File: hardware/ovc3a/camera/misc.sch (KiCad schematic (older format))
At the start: 11 parts, among them CON1 microSD_Card, J5 Conn_02x15_Odd_Even, J6 Conn_02x04_Counter_Clockwise, U9 ARJ11C-MBSAS-A-BA-7MU2

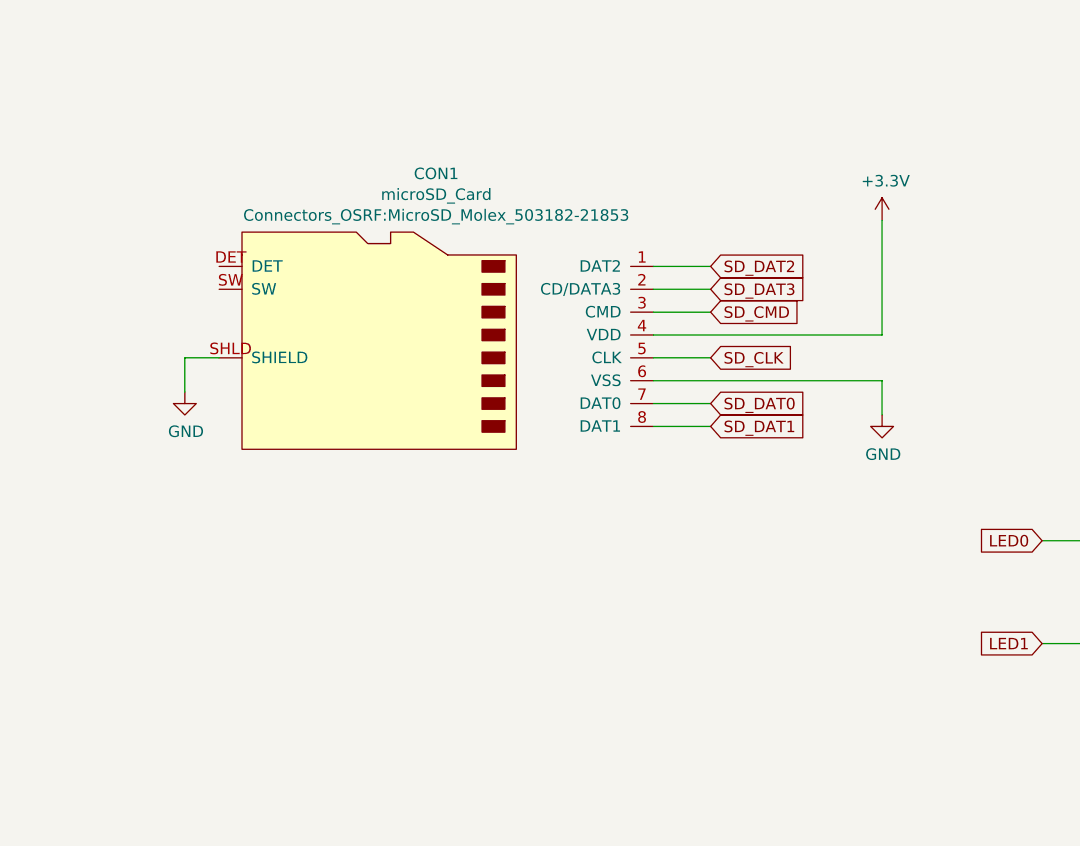
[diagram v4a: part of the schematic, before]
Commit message: switch to in-stock micro-SD connector and do initial pcb route
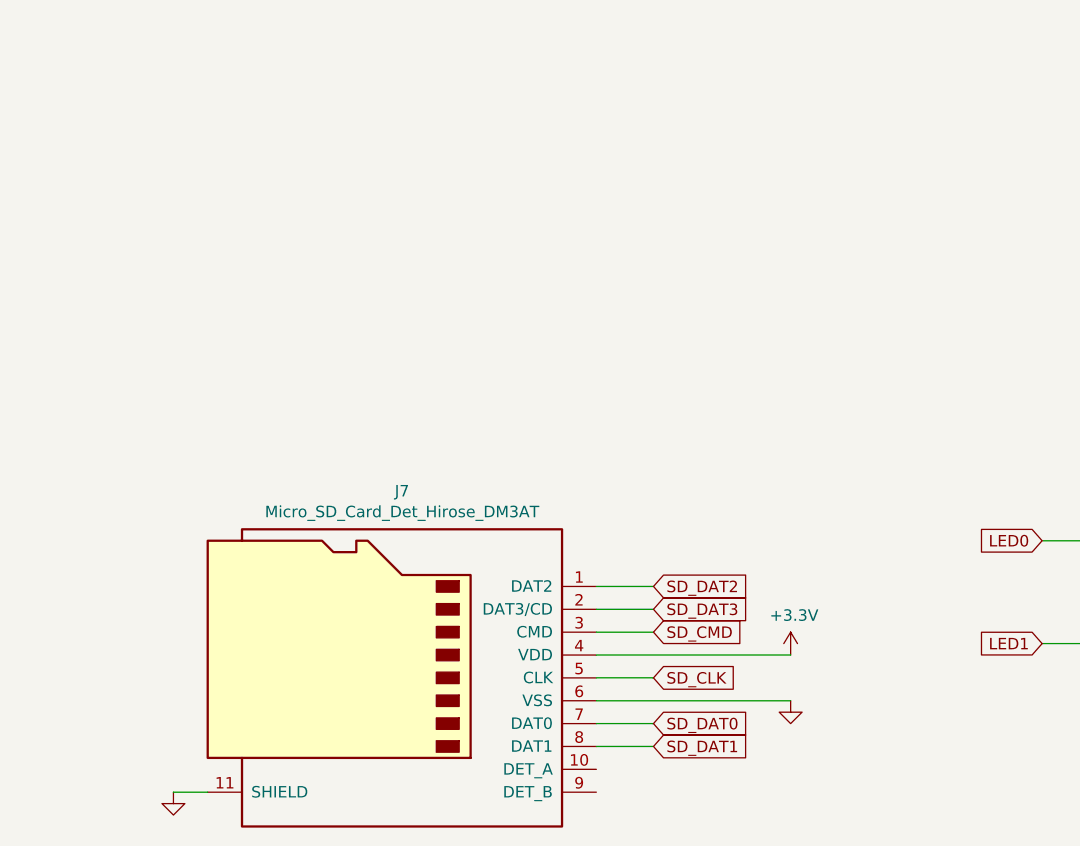
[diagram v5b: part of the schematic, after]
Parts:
- removed CON1: microSD_Card, Connectors_OSRF:MicroSD_Molex_503182-21853, symbol connectors:microSD_Card
- added J7: Micro_SD_Card_Det_Hirose_DM3AT, Connector_Card:microSD_HC_Hirose_DM3AT-SF-PEJM5, symbol Connector:Micro_SD_Card_Det_Hirose_DM3AT
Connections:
- net +3V3: now also J7.4 (VDD)
- net GND: now also J7.11 (SHIELD), J7.6 (VSS)
- net SD_CLK: now also J7.5 (CLK)
- net SD_CMD: now also J7.3 (CMD)
- net SD_DAT0: now also J7.7 (DAT0)
- net SD_DAT1: now also J7.8 (DAT1)
- net SD_DAT2: now also J7.1 (DAT2)
- net SD_DAT3: now also J7.2 (DAT3/CD)
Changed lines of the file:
@@
-	1    0    0    -1
-$EndComp
-$Comp
-L connectors:microSD_Card CON?
-U 1 1 5C477F77
-P 2250 4750
-AR Path="/5C4799A5/5C477F77" Ref="CON?"  Part="1"
-AR Path="/5C470144/5C477F77" Ref="CON1"  Part="1"
-F 0 "CON1" H 2500 5455 50  0000 C CNN
-F 1 "microSD_Card" H 2500 5364 50  0000 C CNN
-F 2 "Connectors_OSRF:MicroSD_Molex_503182-21853" H 2500 5273 50  0000 C CNN
-F 3 "http://www.molex.com/webdocs/datasheets/pdf/en-us/5031821853_MEMORY_CARD_SOCKET.pdf" H 2450 4750 50  0001 C CNN
-F 4 "_" H 2250 4750 50  0001 C CNN "MFN"
-F 5 "_" H 2250 4750 50  0001 C CNN "MFP"
-F 6 "digikey" H 2250 4750 50  0001 C CNN "D1"
-F 7 "mouser" H 2250 4750 50  0001 C CNN "D2"
-F 8 "_" H 2250 4750 50  0001 C CNN "D1PN"
-F 9 "_" H 2250 4750 50  0001 C CNN "D1PL"
-F 10 "_" H 2250 4750 50  0001 C CNN "D2PN"
-F 11 "_" H 2250 4750 50  0001 C CNN "D2PL"
-F 12 "_" H 2250 4750 50  0001 C CNN "Package"
-F 13 "_" H 2250 4750 50  0001 C CNN "Description"
-F 14 "_" H 2250 4750 50  0001 C CNN "Voltage"
-F 15 "_" H 2250 4750 50  0001 C CNN "Power"
-F 16 "_" H 2250 4750 50  0001 C CNN "Tolerance"
-F 17 "_" H 2250 4750 50  0001 C CNN "Temperature"
-F 18 "_" H 2250 4750 50  0001 C CNN "ReverseVoltage"
-F 19 "_" H 2250 4750 50  0001 C CNN "ForwardVoltage"
-F 20 "_" H 2250 4750 50  0001 C CNN "Cont.Current"
-F 21 "_" H 2250 4750 50  0001 C CNN "Frequency"
-F 22 "_" H 2250 4750 50  0001 C CNN "ResonnanceFreq"
-	1    2250 4750
 	1    0    0    -1
 $EndComp
@@
 	3400 1400 3400 1250
 Wire Wire Line
-	3700 4450 3450 4450
-Wire Wire Line
-	3700 4550 3450 4550
-Wire Wire Line
-	3700 4650 3450 4650
-Wire Wire Line
-	3700 5150 3450 5150
-Wire Wire Line
-	3700 5050 3450 5050
-Wire Wire Line
-	3700 4850 3450 4850
-$Comp
-L power:GND #PWR0117
-U 1 1 5C49A0AD
-P 4450 5100
-F 0 "#PWR0117" H 4450 4850 50  0001 C CNN
-F 1 "GND" H 4455 4927 50  0000 C CNN
-F 2 "" H 4450 5100 50  0001 C CNN
-F 3 "" H 4450 5100 50  0001 C CNN
-	1    4450 5100
-	1    0    0    -1
-$EndComp
-Wire Wire Line
-	3450 4750 4450 4750
-Wire Wire Line
-	3450 4950 4450 4950
-Wire Wire Line
-	4450 4950 4450 5100
-$Comp
-L power:GND #PWR0119
-U 1 1 5C49BFA5
-P 1400 5000
-F 0 "#PWR0119" H 1400 4750 50  0001 C CNN
-F 1 "GND" H 1405 4827 50  0000 C CNN
-F 2 "" H 1400 5000 50  0001 C CNN
-F 3 "" H 1400 5000 50  0001 C CNN
-	1    1400 5000
-	1    0    0    -1
-$EndComp
-Wire Wire Line
-	1550 4850 1400 4850
-Wire Wire Line
-	1400 4850 1400 5000
-Wire Wire Line
-	4450 4250 4450 4750
-Text GLabel 3700 4450 2    50   Input ~ 0
+	3450 5850 3200 5850
+Wire Wire Line
+	3450 5950 3200 5950
+Wire Wire Line
+	3450 6050 3200 6050
+Wire Wire Line
+	3450 6550 3200 6550
+Wire Wire Line
+	3450 6450 3200 6450
+Wire Wire Line
+	3450 6250 3200 6250
+Wire Wire Line
+	3200 6150 4050 6150
+Wire Wire Line
+	3200 6350 4050 6350
+Text GLabel 3450 5850 2    50   Input ~ 0
 SD_DAT2
-Text GLabel 3700 4550 2    50   Input ~ 0
+Text GLabel 3450 5950 2    50   Input ~ 0
 SD_DAT3
-Text GLabel 3700 4650 2    50   Input ~ 0
+Text GLabel 3450 6050 2    50   Input ~ 0
 SD_CMD
-Text GLabel 3700 4850 2    50   Input ~ 0
+Text GLabel 3450 6250 2    50   Input ~ 0
 SD_CLK
-Text GLabel 3700 5050 2    50   Input ~ 0
+Text GLabel 3450 6450 2    50   Input ~ 0
 SD_DAT0
-Text GLabel 3700 5150 2    50   Input ~ 0
+Text GLabel 3450 6550 2    50   Input ~ 0
 SD_DAT1
 Text GLabel 3300 1800 2    50   Input ~ 0
@@
 L power:+3.3V #PWR0118
 U 1 1 5C4E6A5A
-P 4450 4250
-F 0 "#PWR0118" H 4450 4100 50  0001 C CNN
-F 1 "+3.3V" H 4465 4423 50  0000 C CNN
-F 2 "" H 4450 4250 50  0001 C CNN
-F 3 "" H 4450 4250 50  0001 C CNN
-	1    4450 4250
+P 4050 6150
+F 0 "#PWR0118" H 4050 6000 50  0001 C CNN
+F 1 "+3.3V" H 4065 6323 50  0000 C CNN
+F 2 "" H 4050 6150 50  0001 C CNN
+F 3 "" H 4050 6150 50  0001 C CNN
+	1    4050 6150
 	1    0    0    -1
 $EndComp
@@
 Text GLabel 7400 3150 2    50   Input ~ 0
 GPIO18
+$Comp
+L Connector:Micro_SD_Card_Det_Hirose_DM3AT J7
+U 1 1 5C4D360F
+P 2300 6250
+F 0 "J7" H 2250 7067 50  0000 C CNN
+F 1 "Micro_SD_Card_Det_Hirose_DM3AT" H 2250 6976 50  0000 C CNN
+F 2 "Connector_Card:microSD_HC_Hirose_DM3AT-SF-PEJM5" H 4350 6950 50  0001 C CNN
+F 3 "https://www.hirose.com/product/en/download_file/key_name/DM3/category/Catalog/doc_file_id/49662/?file_category_id=4&item_id=195&is_series=1" H 2300 6350 50  0001 C CNN
+F 4 "DM3AT-SF-PEJM5" H 2300 6250 50  0001 C CNN "MPN"
+	1    2300 6250
+	-1   0    0    -1
+$EndComp
+$Comp
+L power:GND #PWR0117
+U 1 1 5C49A0AD
+P 4050 6350
+F 0 "#PWR0117" H 4050 6100 50  0001 C CNN
+F 1 "GND" H 4055 6177 50  0001 C CNN
+F 2 "" H 4050 6350 50  0001 C CNN
+F 3 "" H 4050 6350 50  0001 C CNN
+	1    4050 6350
+	1    0    0    -1
+$EndComp
+$Comp
+L power:GND #PWR0119
+U 1 1 5C4F8C21
+P 1350 6750
+F 0 "#PWR0119" H 1350 6500 50  0001 C CNN
+F 1 "GND" H 1355 6577 50  0001 C CNN
+F 2 "" H 1350 6750 50  0001 C CNN
+F 3 "" H 1350 6750 50  0001 C CNN
+	1    1350 6750
+	1    0    0    -1
+$EndComp
+Wire Wire Line
+	1350 6750 1500 6750
 $EndSCHEMATC

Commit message: ovc3a camera pcb work
 * ignore fp-info-cache files
 * reduce size of enet led resistors to 0403.
 * route enet and micro-sd interfaces
 * align lens holders to 90 degrees
 * push outer imagers down a bit to reduce width of pcb to 138mm
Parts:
- C10: footprint Capacitor_SMD:C_0402_1005Metric -> Capacitor_SMD:C_0603_1608Metric
- R12, R13, R14, R15: footprint Resistor_SMD:R_0603_1608Metric -> Resistor_SMD:R_0402_1005Metric
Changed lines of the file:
@@
 F 0 "C10" H 3492 1196 50  0000 L CNN
 F 1 "100n" H 3492 1105 50  0000 L CNN
-F 2 "Capacitor_SMD:C_0402_1005Metric" H 3400 1150 50  0001 C CNN
+F 2 "Capacitor_SMD:C_0603_1608Metric" H 3400 1150 50  0001 C CNN
 F 3 "~" H 3400 1150 50  0001 C CNN
 	1    3400 1150
@@
 F 0 "R13" V 1304 2250 50  0000 C CNN
 F 1 "220R" V 1395 2250 50  0000 C CNN
-F 2 "Resistor_SMD:R_0603_1608Metric" H 1500 2250 50  0001 C CNN
+F 2 "Resistor_SMD:R_0402_1005Metric" H 1500 2250 50  0001 C CNN
 F 3 "~" H 1500 2250 50  0001 C CNN
 	1    1500 2250
@@
 F 0 "R12" V 1304 1700 50  0000 C CNN
 F 1 "220R" V 1395 1700 50  0000 C CNN
-F 2 "Resistor_SMD:R_0603_1608Metric" H 1500 1700 50  0001 C CNN
+F 2 "Resistor_SMD:R_0402_1005Metric" H 1500 1700 50  0001 C CNN
 F 3 "~" H 1500 1700 50  0001 C CNN
 	1    1500 1700
@@
 F 0 "R14" V 5254 5650 50  0000 C CNN
 F 1 "220R" V 5345 5650 50  0000 C CNN
-F 2 "Resistor_SMD:R_0603_1608Metric" H 5450 5650 50  0001 C CNN
+F 2 "Resistor_SMD:R_0402_1005Metric" H 5450 5650 50  0001 C CNN
 F 3 "~" H 5450 5650 50  0001 C CNN
 	1    5450 5650
@@
 F 0 "R15" V 5254 6100 50  0000 C CNN
 F 1 "220R" V 5345 6100 50  0000 C CNN
-F 2 "Resistor_SMD:R_0603_1608Metric" H 5450 6100 50  0001 C CNN
+F 2 "Resistor_SMD:R_0402_1005Metric" H 5450 6100 50  0001 C CNN
 F 3 "~" H 5450 6100 50  0001 C CNN
 	1    5450 6100

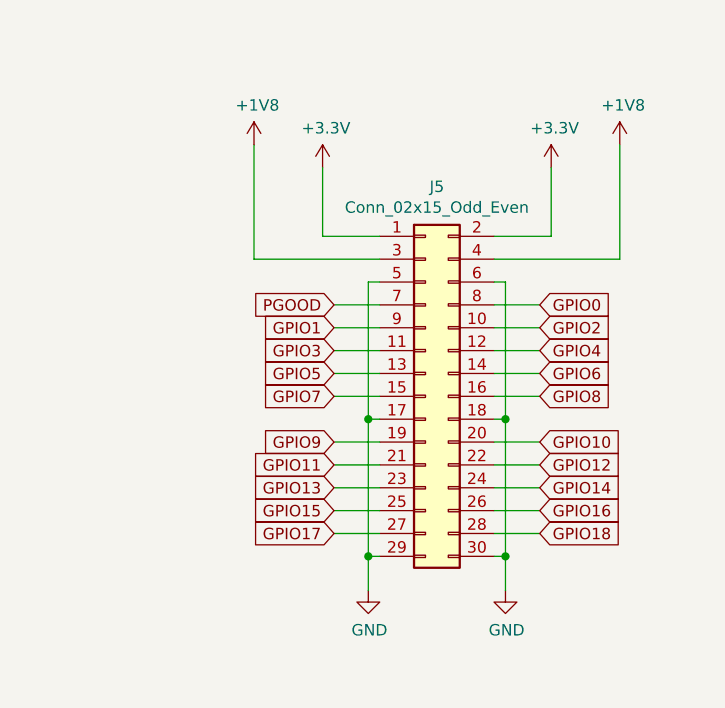
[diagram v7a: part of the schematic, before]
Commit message: Preliminary placement of MIPI lanes, finished routing first imager
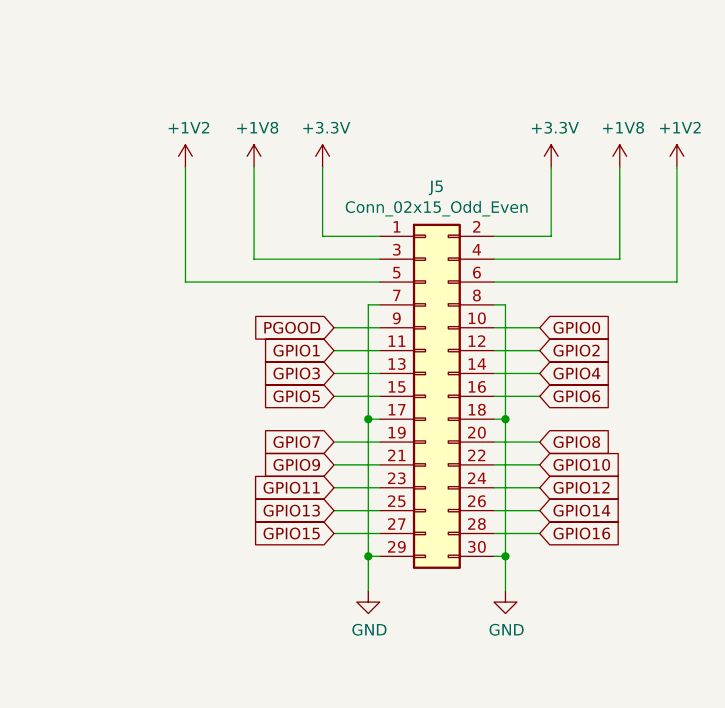
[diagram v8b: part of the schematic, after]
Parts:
- J6: footprint Connector_PinSocket_2.00mm:PinSocket_2x04_P2.00mm_Vertical -> Connector_PinSocket_2.00mm:PinSocket_2x04_P2.00mm_Horizontal
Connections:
- net GPIO17 is gone; now on net GPIO15: J5.27 (Pin_27)
- net GPIO18 is gone; now on net GPIO16: J5.28 (Pin_28)
- net GND: now also J5.7 (Pin_7), J5.8 (Pin_8); no longer J5.5 (Pin_5), J5.6 (Pin_6)
- net GPIO0: now also J5.10 (Pin_10); no longer J5.8 (Pin_8)
- net GPIO1: now also J5.11 (Pin_11); no longer J5.9 (Pin_9)
- net GPIO10: now also J5.22 (Pin_22); no longer J5.20 (Pin_20)
- net GPIO11: now also J5.23 (Pin_23); no longer J5.21 (Pin_21)
- net GPIO12: now also J5.24 (Pin_24); no longer J5.22 (Pin_22)
- net GPIO13: now also J5.25 (Pin_25); no longer J5.23 (Pin_23)
- net GPIO14: now also J5.26 (Pin_26); no longer J5.24 (Pin_24)
- net GPIO15: no longer J5.25 (Pin_25)
- net GPIO16: no longer J5.26 (Pin_26)
- net GPIO2: now also J5.12 (Pin_12); no longer J5.10 (Pin_10)
- net GPIO3: now also J5.13 (Pin_13); no longer J5.11 (Pin_11)
- net GPIO4: now also J5.14 (Pin_14); no longer J5.12 (Pin_12)
- net GPIO5: now also J5.15 (Pin_15); no longer J5.13 (Pin_13)
- net GPIO6: now also J5.16 (Pin_16); no longer J5.14 (Pin_14)
- net GPIO7: now also J5.19 (Pin_19); no longer J5.15 (Pin_15)
- net GPIO8: now also J5.20 (Pin_20); no longer J5.16 (Pin_16)
- net GPIO9: now also J5.21 (Pin_21); no longer J5.19 (Pin_19)
- net PGOOD: now also J5.9 (Pin_9); no longer J5.7 (Pin_7)
- new net +1V2: J5.5 (Pin_5), J5.6 (Pin_6)
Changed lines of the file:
@@
 L power:+1V8 #PWR0140
 U 1 1 5C522639
-P 6150 1450
-F 0 "#PWR0140" H 6150 1300 50  0001 C CNN
-F 1 "+1V8" H 6165 1623 50  0000 C CNN
-F 2 "" H 6150 1450 50  0001 C CNN
-F 3 "" H 6150 1450 50  0001 C CNN
-	1    6150 1450
+P 6150 1550
+F 0 "#PWR0140" H 6150 1400 50  0001 C CNN
+F 1 "+1V8" H 6165 1723 50  0000 C CNN
+F 2 "" H 6150 1550 50  0001 C CNN
+F 3 "" H 6150 1550 50  0001 C CNN
+	1    6150 1550
 	1    0    0    -1
 $EndComp
@@
 L power:+1V8 #PWR0141
 U 1 1 5C522CA8
-P 7750 1450
-F 0 "#PWR0141" H 7750 1300 50  0001 C CNN
-F 1 "+1V8" H 7765 1623 50  0000 C CNN
-F 2 "" H 7750 1450 50  0001 C CNN
-F 3 "" H 7750 1450 50  0001 C CNN
-	1    7750 1450
+P 7750 1550
+F 0 "#PWR0141" H 7750 1400 50  0001 C CNN
+F 1 "+1V8" H 7765 1723 50  0000 C CNN
+F 2 "" H 7750 1550 50  0001 C CNN
+F 3 "" H 7750 1550 50  0001 C CNN
+	1    7750 1550
 	1    0    0    -1
 $EndComp
@@
 	7200 1950 7750 1950
 Wire Wire Line
-	7750 1950 7750 1450
-Wire Wire Line
 	6700 1950 6150 1950
-Wire Wire Line
-	6150 1950 6150 1450
 $Comp
 L power:GND #PWR0143
@@
 	1    0    0    -1
 $EndComp
-Text GLabel 6500 2150 0    50   Input ~ 0
+Text GLabel 6500 2250 0    50   Input ~ 0
 PGOOD
-Wire Wire Line
-	6650 2050 6650 2650
-Wire Wire Line
-	6650 2050 6700 2050
 Wire Wire Line
 	6700 2650 6650 2650
@@
 Wire Wire Line
 	6650 3250 6650 3400
-Wire Wire Line
-	7250 2050 7250 2650
 $Comp
 L power:GND #PWR0142
@@
 Connection ~ 7250 2650
 Wire Wire Line
-	7250 2650 7250 3250
-Wire Wire Line
-	7200 2050 7250 2050
-Wire Wire Line
-	6700 2150 6500 2150
+	6700 2250 6500 2250
 Wire Wire Line
 	6700 1850 6450 1850
@@
 F 0 "J6" H 7100 5100 50  0000 C CNN
 F 1 "Conn_02x04_Counter_Clockwise" H 7400 5000 50  0000 C CNN
-F 2 "Connector_PinSocket_2.00mm:PinSocket_2x04_P2.00mm_Vertical" H 7000 4750 50  0001 C CNN
+F 2 "Connector_PinSocket_2.00mm:PinSocket_2x04_P2.00mm_Horizontal" H 7000 4750 50  0001 C CNN
 F 3 "~" H 7000 4750 50  0001 C CNN
 	1    7000 4750
@@
 	5350 6100 5150 6100
 Wire Wire Line
-	6500 2250 6700 2250
-Text GLabel 6500 2350 0    50   Input ~ 0
-GPIO3
-Wire Wire Line
 	6500 2350 6700 2350
 Text GLabel 6500 2450 0    50   Input ~ 0
-GPIO5
+GPIO3
 Wire Wire Line
 	6500 2450 6700 2450
 Text GLabel 6500 2550 0    50   Input ~ 0
-GPIO7
+GPIO5
 Wire Wire Line
 	6500 2550 6700 2550
 Text GLabel 6500 2750 0    50   Input ~ 0
-GPIO9
+GPIO7
 Wire Wire Line
 	6500 2750 6700 2750
 Text GLabel 6500 2850 0    50   Input ~ 0
+GPIO9
+Wire Wire Line
+	6500 2850 6700 2850
+Text GLabel 6500 2950 0    50   Input ~ 0
 GPIO11
 Wire Wire Line
-	6500 2850 6700 2850
-Wire Wire Line
 	6500 2950 6700 2950
 Wire Wire Line
@@
 Wire Wire Line
 	6500 3150 6700 3150
-Text GLabel 7400 2150 2    50   Input ~ 0
+Text GLabel 7400 2250 2    50   Input ~ 0
 GPIO0
-Wire Wire Line
-	7400 2150 7200 2150
-Text GLabel 7400 2250 2    50   Input ~ 0
-GPIO2
 Wire Wire Line
 	7400 2250 7200 2250
 Text GLabel 7400 2350 2    50   Input ~ 0
-GPIO4
+GPIO2
 Wire Wire Line
 	7400 2350 7200 2350
 Text GLabel 7400 2450 2    50   Input ~ 0
-GPIO6
+GPIO4
 Wire Wire Line
 	7400 2450 7200 2450
 Text GLabel 7400 2550 2    50   Input ~ 0
-GPIO8
+GPIO6
 Wire Wire Line
 	7400 2550 7200 2550
-Text GLabel 7400 2750 2    50   Input ~ 0
+Text GLabel 7400 2850 2    50   Input ~ 0
 GPIO10
 Wire Wire Line
-	7400 2750 7200 2750
-Wire Wire Line
 	7400 2850 7200 2850
 Wire Wire Line
@@
 Wire Wire Line
 	7400 3150 7200 3150
-Text GLabel 6500 2250 0    50   Input ~ 0
+Text GLabel 6500 2350 0    50   Input ~ 0
 GPIO1
-Text GLabel 6500 2950 0    50   Input ~ 0
+Text GLabel 6500 3050 0    50   Input ~ 0
 GPIO13
-Text GLabel 6500 3050 0    50   Input ~ 0
+Text GLabel 6500 3150 0    50   Input ~ 0
 GPIO15
-Text GLabel 6500 3150 0    50   Input ~ 0
-GPIO17
-Text GLabel 7400 2850 2    50   Input ~ 0
+Text GLabel 7400 2950 2    50   Input ~ 0
 GPIO12
-Text GLabel 7400 2950 2    50   Input ~ 0
+Text GLabel 7400 3050 2    50   Input ~ 0
 GPIO14
-Text GLabel 7400 3050 2    50   Input ~ 0
+Text GLabel 7400 3150 2    50   Input ~ 0
 GPIO16
-Text GLabel 7400 3150 2    50   Input ~ 0
-GPIO18
 $Comp
 L Connector:Micro_SD_Card_Det_Hirose_DM3AT J7
@@
 Wire Wire Line
 	1350 6750 1500 6750
+Wire Wire Line
+	7250 2650 7250 3250
+Wire Wire Line
+	7400 2750 7200 2750
+Text GLabel 7400 2750 2    50   Input ~ 0
+GPIO8
+Wire Wire Line
+	6700 2150 6650 2150
+Wire Wire Line
+	6650 2150 6650 2650
+Wire Wire Line
+	7200 2150 7250 2150
+Wire Wire Line
+	7250 2150 7250 2650
+$Comp
+L power:+1V2 #PWR0232
+U 1 1 5CA0D06A
+P 8000 1550
+F 0 "#PWR0232" H 8000 1400 50  0001 C CNN
+F 1 "+1V2" H 8015 1723 50  0000 C CNN
+F 2 "" H 8000 1550 50  0001 C CNN
+F 3 "" H 8000 1550 50  0001 C CNN
+	1    8000 1550
+	1    0    0    -1
+$EndComp
+Wire Wire Line
+	7750 1550 7750 1950
+Wire Wire Line
+	6150 1550 6150 1950
+$Comp
+L power:+1V2 #PWR0233
+U 1 1 5CA12CD0
+P 5850 1550
+F 0 "#PWR0233" H 5850 1400 50  0001 C CNN
+F 1 "+1V2" H 5865 1723 50  0000 C CNN
+F 2 "" H 5850 1550 50  0001 C CNN
+F 3 "" H 5850 1550 50  0001 C CNN
+	1    5850 1550
+	1    0    0    -1
+$EndComp
+Wire Wire Line
+	5850 1550 5850 2050
+Wire Wire Line
+	5850 2050 6700 2050
+Wire Wire Line
+	7200 2050 8000 2050
+Wire Wire Line
+	8000 2050 8000 1550
 $EndSCHEMATC
